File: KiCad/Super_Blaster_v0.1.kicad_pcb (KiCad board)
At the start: 4 copper layers, 27 x 59 mm, 13 parts, among them J1 USB_TypeC_AMP_12401610E4#2A, J2 CONN_02X20, J3 CONN_02X20, J4 CONN_02X20, U1 LM324, U2 iCE40-HX8K-CT256, U3 FUSB340, U4 FT601Q

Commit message: top routed?
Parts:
- removed J3, J4: CONN_02X20, Pin_Headers:Pin_Header_Straight_2x20_Pitch1.27mm
- added C1: .1u, Capacitors_SMD:C_0402, F.Cu at (105.8, 154.0)
- added C2: .1u, Capacitors_SMD:C_0402, F.Cu at (103.7, 156.3)
- added C3: .1u, Capacitors_SMD:C_0402, F.Cu at (122.2, 153.8)
- added C4: .1u, Capacitors_SMD:C_0402, F.Cu at (123.7, 156.9)
- added C5: .1u, Capacitors_SMD:C_0402, F.Cu at (106.4, 157.0)
- added C6: 18p, Capacitors_SMD:C_0402, B.Cu at (116.6, 153.9)
- added C7: 18p, Capacitors_SMD:C_0402, F.Cu at (125.0, 152.4)
- added C9: .1uF, Capacitors_SMD:C_0402, F.Cu at (119.6, 154.0)
- added M1: CLOCK_EN, Crystals:Crystal_SMD_EuroQuartz_MT-4pin_3.2x2.5mm, B.Cu at (114.0, 114.0)
- added R1: 5.1K_10%, Resistors_SMD:R_0402, B.Cu at (112.8, 153.0)
- added R2: ?, Resistors_SMD:R_0402, F.Cu at (125.4, 149.3)
- added R3: ?, Resistors_SMD:R_0402, F.Cu at (123.7, 149.3)
- added R4: ?, Resistors_SMD:R_0402, F.Cu at (121.9, 149.3)
- added R5: ?, Resistors_SMD:R_0402, F.Cu at (120.4, 149.4)
- added R6: 5.1K_10%, Resistors_SMD:R_0402, B.Cu at (114.0, 153.0)
- added R7: 10K, Resistors_SMD:R_0402, F.Cu at (120.7, 151.7)
- added R8: 1.6K 1%, Resistors_SMD:R_0402, F.Cu at (110.1, 147.5)
- added RN1: 1M, Resistors_SMD:R_Array_Concave_4x0402, B.Cu at (104.1, 144.0)
- added Y1: 30MHz, Crystals:Crystal_SMD_MicroCrystal_CC1V-T1A-2pin_8.0x3.7mm, F.Cu at (129.7, 142.8)
- C8: moved to B.Cu
- R10, R9: footprint Resistors_SMD:R_0603 -> Resistors_SMD:R_0402
- moved R10 42.8 mm to (120.5, 157.0), turned to 0 degrees
- moved R9 42.0 mm to (109.6, 153.7), turned to 0 degrees
- moved D1 27.0 mm to (101.7, 153.1), turned to 0 degrees
- moved C8 19.0 mm to (113.1, 155.4), turned to 0 degrees
- moved U3 1.99 mm to (114.7, 144.3), turned to 225 degrees
- moved U2 1.00 mm to (113.5, 115.0), turned to 315 degrees
- moved U4 0.81 mm to (113.5, 134.3), turned to 45 degrees
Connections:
- net /Bottom_Interface/BE_0 renamed Net-(U2-PadN6)
- net /Bottom_Interface/BE_1 renamed Net-(U2-PadT1)
- net /Bottom_Interface/BE_2 renamed Net-(U2-PadP4)
- net /Bottom_Interface/BE_3 renamed Net-(U2-PadR2)
- net /Bottom_Interface/CBSEL_0 renamed /CBSEL_0
- net /Bottom_Interface/CBSEL_1 renamed /CBSEL_1
- net /USB_Connection/1.5A_DET renamed /1.5A_DET
- net /USB_Connection/3A_DET renamed /3A_DET
- net /USB_Connection/BE_0 renamed BE_0
- net /USB_Connection/BE_1 renamed BE_1
- net /USB_Connection/BE_2 renamed BE_2
- net /USB_Connection/BE_3 renamed BE_3
- net /USB_Connection/GPIO0 renamed /GPIO0
- net /USB_Connection/GPIO1 renamed /GPIO1
- net /USB_Connection/SS_RX+ renamed /USB_Connection/SS_RX_P
- net /USB_Connection/SS_RX- renamed /USB_Connection/SS_RX_N
- net /USB_Connection/SS_RX1+ renamed /USB_Connection/SS_RX1_P
- net /USB_Connection/SS_RX1- renamed /USB_Connection/SS_RX1_N
- net /USB_Connection/SS_TX+ renamed /USB_Connection/SS_TX_P
- net /USB_Connection/SS_TX- renamed /USB_Connection/SS_TX_N
- net /USB_Connection/USB_D+ renamed /USB_Connection/USB_D_P
- net /USB_Connection/USB_D- renamed /USB_Connection/USB_D_N
- net /USB_Connection/~SIWU renamed /~SIWU
- J1 pad A10: /USB_Connection/SS_RX2- -> /USB_Connection/SS_RX2_N
- J1 pad A11: /USB_Connection/SS_RX2+ -> /USB_Connection/SS_RX2_P
- J1 pad A2: /USB_Connection/SS_TX1+ -> /USB_Connection/SS_TX1_P
- J1 pad A3: /USB_Connection/SS_TX1- -> /USB_Connection/SS_TX1_N
- J1 pad B2: /USB_Connection/SS_TX2- -> /USB_Connection/SS_TX2_N
- J1 pad B3: /USB_Connection/SS_TX2+ -> /USB_Connection/SS_TX2_P
- R9 pad 2: /Bottom_Interface/~CRESET -> /~CRESET
- U2 pad A12: Net-(U2-PadA12) -> Earth
- U2 pad A4: Net-(U2-PadA12) -> Earth
- U2 pad C15: Net-(U2-PadC15) -> 3v3
- U2 pad E1: Net-(U2-PadE1) -> 3v3
- U2 pad E15: Net-(U2-PadA12) -> Earth
- U2 pad E16: Net-(U2-PadE16) -> D0
- U2 pad E7: Net-(U2-PadE7) -> Earth
- U2 pad F15: Net-(U2-PadF15) -> D2
- U2 pad F16: Net-(U2-PadF16) -> D1
- U2 pad G15: Net-(U2-PadG15) -> D4
- U2 pad G16: Net-(U2-PadG16) -> D3
- U2 pad G6: Net-(U2-PadE1) -> 3v3
- U2 pad G7: Net-(U2-PadA12) -> Earth
- U2 pad G8: Net-(U2-PadA12) -> Earth
- U2 pad G9: Net-(U2-PadA12) -> Earth
- U2 pad H10: Net-(U2-PadC15) -> 3v3
- U2 pad H15: Net-(U2-PadC15) -> 3v3
- U2 pad H7: Net-(U2-PadA12) -> Earth
- U2 pad H8: Net-(U2-PadA12) -> Earth
- U2 pad H9: Net-(U2-PadA12) -> Earth
- U2 pad J15: Net-(U2-PadJ15) -> D6
- U2 pad J16: Net-(U2-PadJ16) -> D5
- U2 pad J6: Net-(U2-PadE1) -> 3v3
- U2 pad J7: Net-(U2-PadA12) -> Earth
- U2 pad J8: Net-(U2-PadA12) -> Earth
- U2 pad J9: Net-(U2-PadA12) -> Earth
- U2 pad K15: Net-(U2-PadK15) -> D8
- U2 pad K16: Net-(U2-PadK16) -> D7
- U2 pad K2: Net-(U2-PadA12) -> Earth
- U2 pad K7: Net-(U2-PadA12) -> Earth
- U2 pad K9: /Bottom_Interface/GBIN4 -> /Bottom_Interface/50MHz
- U2 pad L10: D13 -> Net-(U2-PadL10)
- U2 pad L11: D3 -> Net-(U2-PadL11)
- U2 pad L15: Net-(U2-PadA12) -> Earth
- U2 pad L16: Net-(U2-PadL16) -> D9
- U2 pad L9: D22 -> Net-(U2-PadL9)
- U2 pad M11: D6 -> Net-(U2-PadM11)
- U2 pad M12: D1 -> Net-(U2-PadM12)
- U2 pad M15: Net-(U2-PadM15) -> D11
- U2 pad M16: Net-(U2-PadM16) -> D10
- U2 pad M7: D30 -> Net-(U2-PadM7)
- U2 pad M8: D27 -> Net-(U2-PadM8)
- U2 pad M9: D16 -> Net-(U2-PadM9)
- U2 pad N1: Net-(U2-PadE1) -> 3v3
- U2 pad N10: D11 -> Net-(U2-PadN10)
- U2 pad N11: /Bottom_Interface/~CRESET -> Net-(U2-PadN11)
- U2 pad N12: D4 -> Net-(U2-PadN12)
- U2 pad N15: Net-(U2-PadC15) -> 3v3
- U2 pad N16: Net-(U2-PadN16) -> D12
- U2 pad N5: /Bottom_Interface/~TXE -> Net-(U2-PadN5)
- U2 pad N7: D29 -> Net-(U2-PadN7)
- U2 pad N8: Net-(U2-PadN8) -> Earth
- U2 pad N9: D18 -> Net-(U2-PadN9)
- U2 pad P10: D12 -> Net-(U2-PadP10)
- U2 pad P15: Net-(U2-PadP15) -> D13
- U2 pad P16: Net-(U2-PadP16) -> D14
- U2 pad P5: /Bottom_Interface/~WR -> Net-(U2-PadP5)
- U2 pad P6: D28 -> Net-(U2-PadP6)
- U2 pad P7: D19 -> Net-(U2-PadP7)
- U2 pad P8: D24 -> Net-(U2-PadP8)
- U2 pad P9: D15 -> Net-(U2-PadP9)
- U2 pad R10: D14 -> D22
- U2 pad R15: Net-(U2-PadR15) -> D15
- U2 pad R16: D0 -> D16
- U2 pad R3: /Bottom_Interface/~RD -> Net-(U2-PadR3)
- U2 pad R5: /Bottom_Interface/~OE -> D29
- U2 pad R6: D25 -> D27
- U2 pad R7: Net-(U2-PadA12) -> Earth
- U2 pad T10: D10 -> D23
- U2 pad T11: D9 -> D21
- U2 pad T12: Net-(U2-PadA12) -> Earth
- U2 pad T13: D5 -> D20
- U2 pad T14: D7 -> D19
- U2 pad T15: D8 -> D18
- U2 pad T16: D2 -> D17
- U2 pad T2: /Bottom_Interface/~RXF -> Net-(U2-PadT2)
- U2 pad T3: /Bottom_Interface/~Wakeup -> Net-(U2-PadT3)
- U2 pad T4: Net-(U2-PadA12) -> Earth
- U2 pad T5: D26 -> D30
- U2 pad T6: D23 -> D28
- U2 pad T7: D21 -> D26
- U2 pad T8: D20 -> D25
- U2 pad T9: D17 -> D24
- U4 pad 15: /USB_Connection/~Reset -> /~RESET
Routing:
- net D13: track 0.00 -> 23.4 mm
- net D20: track 0.00 -> 23.0 mm
- net D16: track 0.00 -> 23.0 mm
- net D17: track 0.00 -> 23.0 mm
- net D19: track 0.00 -> 23.0 mm
- net D22: track 0.00 -> 23.0 mm
- net D15: track 0.00 -> 23.0 mm
- net D10: track 0.00 -> 23.0 mm
- net D14: track 0.00 -> 23.0 mm
- net D9: track 0.00 -> 23.0 mm
- net D11: track 0.00 -> 23.0 mm
- net D12: track 0.00 -> 23.0 mm
- net D18: track 0.00 -> 23.0 mm
- net D8: track 0.00 -> 23.0 mm
- net D21: track 0.00 -> 22.9 mm
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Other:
- net class 4mil added: clearance 0.1016, trace_width 0.1016, via_dia 0.45, via_drill 0.3
- net class 5 mil added: clearance 0.127, trace_width 0.127, via_dia 0.45, via_drill 0.3
- net class Data_Bus added: clearance 0.127, trace_width 0.127, via_dia 0.4572, via_drill 0.254
- net class Data_EN added: clearance 0.127, trace_width 0.127, via_dia 0.4572, via_drill 0.254
- net class Default: clearance 0.2 -> 0.1016; trace_width 0.25 -> 0.127; via_dia 0.6 -> 0.4572; via_drill 0.4 -> 0.254
- rule pad_to_mask_clearance: 0.2 -> 0.1
- rule trace_clearance: 0.2 -> 0.1016
- rule trace_min: 0.2 -> 0.1016
- rule via_min_drill: 0.3 -> 0
- rule via_min_size: 0.4 -> 0

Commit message: 10_20_2017 update
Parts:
- added J3: CONN_02X10, Pin_Headers:Pin_Header_Straight_2x10_Pitch1.27mm, F.Cu at (127.2, 101.0)
- added J4: CONN_02X10, Pin_Headers:Pin_Header_Straight_2x10_Pitch1.27mm, F.Cu at (101.5, 114.3)
- J2: value CONN_02X20 -> CONN_02X10; footprint Pin_Headers:Pin_Header_Straight_2x20_Pitch1.27mm -> Pin_Headers:Pin_Header_Straight_2x10_Pitch1.27mm
- M1: footprint Crystals:Crystal_SMD_EuroQuartz_MT-4pin_3.2x2.5mm -> Crystals:Crystal_SMD_2520-4pin_2.5x2.0mm
- U1: footprint SMD_Packages:SOIC-14_N -> Homebrew:Homebrew-HV-QFN-16; moved to B.Cu
- Y1: moved to B.Cu
- moved D1 51.4 mm to (146.1, 127.3), turned to 180 degrees
- moved R1 49.8 mm to (134.0, 108.0)
- moved R7 48.3 mm to (138.3, 106.8)
- moved C7 46.2 mm to (139.6, 108.6)
- moved R10 43.7 mm to (143.3, 119.8), turned to 180 degrees
- moved R9 39.5 mm to (138.2, 126.5), turned to 180 degrees
- moved C9 34.7 mm to (134.6, 122.8), turned to 180 degrees
- moved C4 25.2 mm to (112.6, 134.3), turned to 270 degrees
- moved R3 25.0 mm to (103.4, 134.7), turned to 90 degrees
- moved R2 24.9 mm to (105.3, 134.6), turned to 270 degrees
- moved R6 24.4 mm to (97.2, 135.3)
- moved R5 24.3 mm to (104.7, 130.8)
- moved R4 24.3 mm to (104.7, 132.1), turned to 180 degrees
- moved C2 24.1 mm to (113.4, 134.3), turned to 90 degrees
- moved C1 22.2 mm to (115.4, 134.0), turned to 135 degrees
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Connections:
- net Net-(C1-Pad2) renamed /USB_Connection/T2_N
- net Net-(C2-Pad2) renamed /USB_Connection/T1_N
- net Net-(C3-Pad1) renamed /USB_Connection/T2_P
- net Net-(C4-Pad1) renamed /USB_Connection/T1_P
- net Net-(C6-Pad1) renamed /USB_Connection/Xo
- net Net-(C7-Pad2) renamed /USB_Connection/Xi
- U3 pad 8: /USB_Connection/SS_RX2+ -> /USB_Connection/SS_RX2_P
- U3 pad 9: /USB_Connection/SS_RX2- -> /USB_Connection/SS_RX2_N
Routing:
- net Earth: track 0.00 -> 29.8 mm, vias 0 -> 12
- net /USB_Connection/USB_D_N: track 0.00 -> 20.7 mm
- net /USB_Connection/USB_D_P: track 0.00 -> 19.8 mm, vias 0 -> 2
- net D17: track 23.0 -> 3.38 mm
- net D16: track 23.0 -> 3.54 mm
- net D18: track 23.0 -> 4.34 mm
- net D14: track 23.0 -> 4.92 mm
- net D15: track 23.0 -> 5.13 mm
- net D19: track 23.0 -> 5.31 mm
- net D12: track 23.0 -> 5.95 mm
- net D13: track 23.4 -> 6.41 mm
- net D20: track 23.0 -> 6.28 mm
- net D10: track 23.0 -> 7.09 mm
- net D11: track 23.0 -> 7.45 mm
- net D9: track 23.0 -> 7.87 mm
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- added copper zone on In2.Cu, net 3v3
- added copper zone on In1.Cu, net Earth
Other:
- board size 27 x 59 mm -> 30 x 45 mm
- net class Default: clearance 0.1016 -> 0.127
- rule pad_to_mask_clearance: 0.1 -> 0.0762
- rule trace_clearance: 0.1016 -> 0.127
- board text added: "3.3V power"
- board text added: "VLeft"
- board text added: "VRight"

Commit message: 12_11_17 update
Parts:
- added C10: .1uF, Capacitors_SMD:C_0402, F.Cu at (136.6, 140.4)
- added C11: 1nF, Capacitors_SMD:C_0402, F.Cu at (140.1, 140.4)
- added R11: 1M, Resistors_SMD:R_0402, F.Cu at (133.2, 140.5)
- C6: moved to F.Cu
- Y1: footprint Crystals:Crystal_SMD_MicroCrystal_CC1V-T1A-2pin_8.0x3.7mm -> Crystals:Crystal_SMD_2016-4pin_2.0x1.6mm; moved to F.Cu
- moved C7 32.2 mm to (119.7, 133.9), turned to 135 degrees
- moved Y1 12.8 mm to (120.9, 136.0), turned to 180 degrees
- moved C6 9.10 mm to (120.9, 133.2), turned to 135 degrees
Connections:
- C5 pad 1: Earth -> GND
- C6 pad 1: /USB_Connection/Xo -> GND
- C6 pad 2: Earth -> /USB_Connection/Xo
- C7 pad 1: Earth -> GND
- C8 pad 2: Earth -> GND
- J1 pad A1: Earth -> GND
- J1 pad A12: Earth -> GND
- J1 pad A4: /USB_Connection/USB_V -> USB_V
- J1 pad A9: /USB_Connection/USB_V -> USB_V
- J1 pad B1: Earth -> GND
- J1 pad B12: Earth -> GND
- J1 pad B4: /USB_Connection/USB_V -> USB_V
- J1 pad B9: /USB_Connection/USB_V -> USB_V
- J3 pad 15: Net-(J3-Pad15) -> USB_V
- J3 pad 16: Net-(J3-Pad16) -> USB_V
- J3 pad 17: Net-(J3-Pad17) -> 3v3
- J3 pad 18: Net-(J3-Pad18) -> 3v3
- J3 pad 19: Net-(J3-Pad19) -> GND
- J3 pad 20: Net-(J3-Pad20) -> GND
- R1 pad 2: Earth -> GND
- R6 pad 2: Earth -> GND
- R8 pad 2: Earth -> GND
- U2 pad A12: Earth -> GND
- U2 pad A4: Earth -> GND
- U2 pad E15: Earth -> GND
- U2 pad E7: Earth -> Net-(U2-PadE7)
- U2 pad G7: Earth -> GND
- U2 pad G8: Earth -> GND
- U2 pad G9: Earth -> GND
- U2 pad H7: Earth -> GND
- U2 pad H8: Earth -> GND
- U2 pad H9: Earth -> GND
- U2 pad J7: Earth -> GND
- U2 pad J8: Earth -> GND
- U2 pad J9: Earth -> GND
- U2 pad K2: Earth -> GND
- U2 pad K7: Earth -> GND
- U2 pad L15: Earth -> GND
- U2 pad N8: Earth -> Net-(U2-PadE7)
- U2 pad R7: Earth -> GND
- U2 pad T12: Earth -> GND
- U2 pad T4: Earth -> GND
- U3 pad 12: Earth -> GND
- U3 pad 18: Earth -> GND
- U3 pad 3: Earth -> GND
- U3 pad 7: Earth -> GND
- U3 pad PAD: Earth -> GND
- U4 pad 1: Earth -> GND
- U4 pad 26: Earth -> GND
- U4 pad 29: Earth -> GND
- U4 pad 36: Earth -> GND
- U4 pad 77: Earth -> GND
- Y1 pad 1: /USB_Connection/Xi -> /USB_Connection/Xo
- Y1 pad 2: /USB_Connection/Xo -> GND
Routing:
- net Earth: track 29.8 -> 0.00 mm, vias 12 -> 0
- net GND: track 0.00 -> 28.7 mm, vias 0 -> 10
- net /USB_Connection/Xi: track 0.00 -> 6.24 mm
- net /USB_Connection/Xo: track 0.00 -> 5.50 mm
- net /USB_Connection/USB_D_N: track 20.7 -> 22.6 mm
- net /USB_Connection/USB_D_P: track 19.8 -> 21.5 mm
- net Net-(U2-PadE7): track 0.00 -> 1.07 mm, vias 0 -> 2
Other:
- net class Default: clearance 0.127 -> 0.1524
- rule trace_clearance: 0.127 -> 0.1524

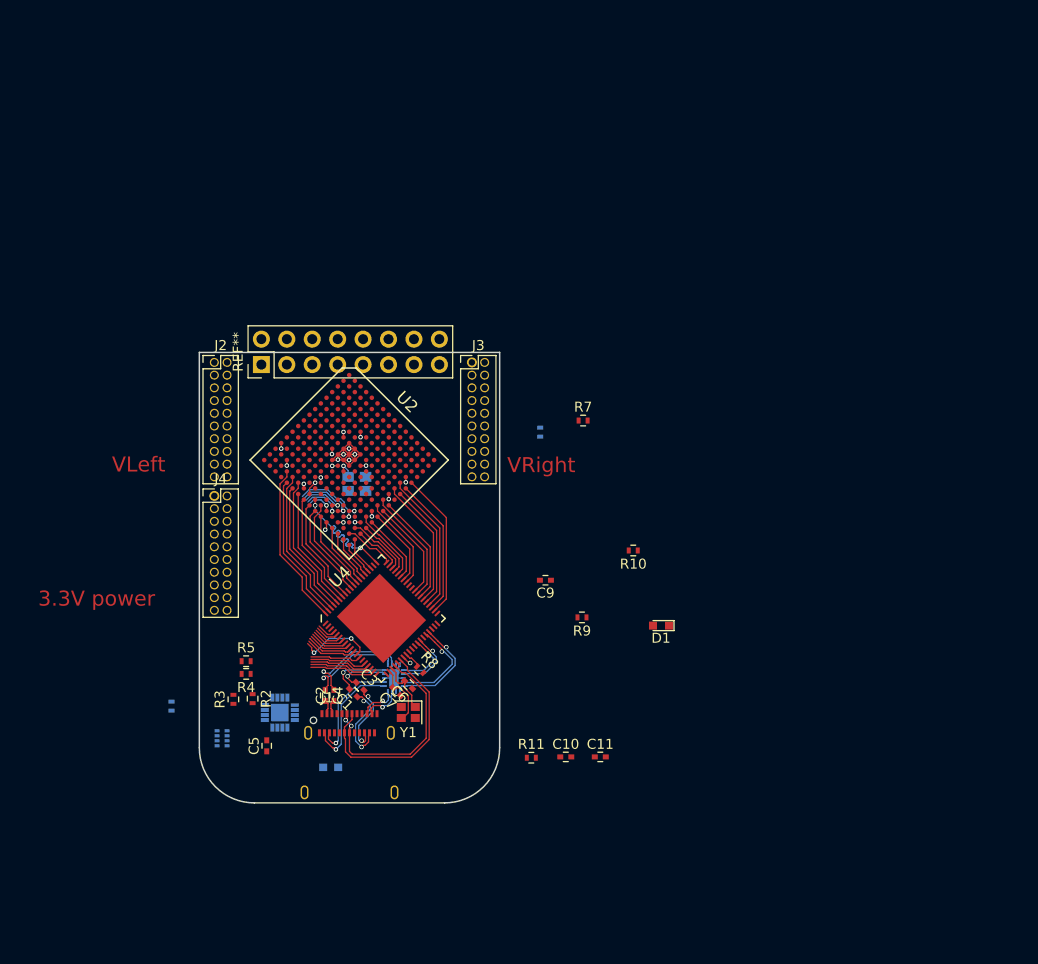
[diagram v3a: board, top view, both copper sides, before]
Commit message: switch to beaglepocket outline
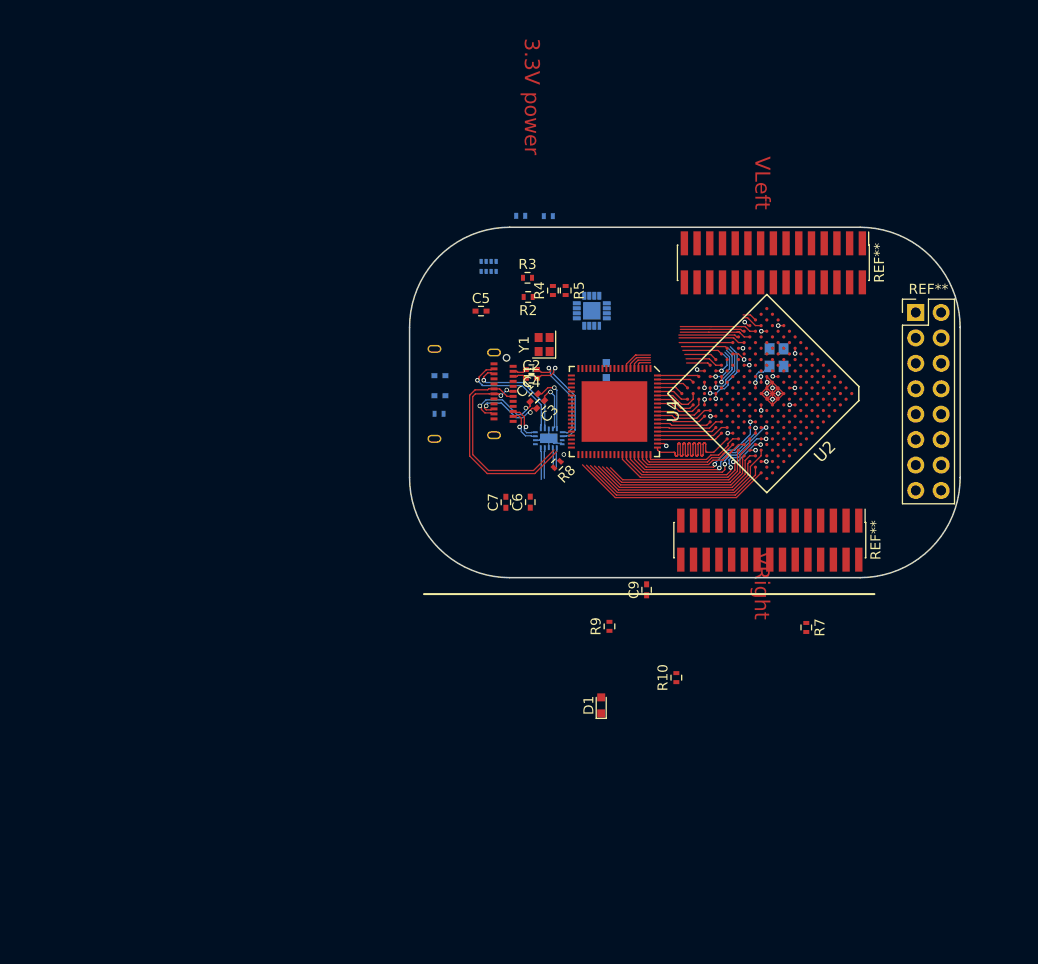
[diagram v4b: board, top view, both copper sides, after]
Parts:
- removed J2, J3, J4: CONN_02X10, Pin_Headers:Pin_Header_Straight_2x10_Pitch1.27mm
- added REF**: Pin_Header_Straight_2x15_Pitch1.27mm_SMD, Pin_Headers:Pin_Header_Straight_2x15_Pitch1.27mm_SMD, F.Cu at (157.3, 91.1)
- added REF**: Pin_Header_Straight_2x15_Pitch1.27mm_SMD, Pin_Headers:Pin_Header_Straight_2x15_Pitch1.27mm_SMD, F.Cu at (157.0, 118.8)
- C10, C11, R11: moved to B.Cu
- moved REF** 65.6 mm to (171.6, 96.0), turned to 0 degrees
- moved R6 60.1 mm to (132.1, 86.4), turned to 180 degrees
- moved RN1 54.1 mm to (128.9, 91.4), turned to 270 degrees
- moved R3 51.3 mm to (132.8, 92.5), turned to 0 degrees
- moved U1 50.8 mm to (139.2, 95.8), turned to 180 degrees
- moved R4 49.1 mm to (135.3, 93.8), turned to 90 degrees
- moved R5 48.9 mm to (136.6, 93.8), turned to 270 degrees
- moved R2 48.7 mm to (132.8, 94.5), turned to 180 degrees
- moved C5 48.4 mm to (128.1, 95.9), turned to 0 degrees
- moved C8 48.3 mm to (140.7, 101.8), turned to 90 degrees
- moved M1 43.8 mm to (157.7, 100.5), turned to 270 degrees
- moved U2 42.2 mm to (156.7, 104.1), turned to 225 degrees
- moved C11 41.3 mm to (124.0, 102.3), turned to 180 degrees
- moved Y1 39.2 mm to (134.4, 99.2), turned to 90 degrees
- moved C4 38.5 mm to (133.2, 101.7), turned to 180 degrees
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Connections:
- C9 pad 2: Earth -> GND
- M1 pad 2: Earth -> GND
- R3 pad 2: Earth -> GND
- R5 pad 2: Earth -> GND
- RN1 pad 3: Earth -> GND
- U1 pad 11: Earth -> GND
- U2 pad B16: Net-(U2-PadB16) -> D0
- U2 pad C16: Net-(U2-PadC16) -> D1
- U2 pad D14: Net-(U2-PadD14) -> D2
- U2 pad D15: Net-(U2-PadD15) -> D4
- U2 pad D16: Net-(U2-PadD16) -> D3
- U2 pad E13: Net-(U2-PadE13) -> D9
- U2 pad E14: Net-(U2-PadE14) -> D8
- U2 pad E16: D0 -> D5
- U2 pad F12: Net-(U2-PadF12) -> D10
- U2 pad F13: Net-(U2-PadF13) -> D11
- U2 pad F14: Net-(U2-PadF14) -> D6
- U2 pad F15: D2 -> D13
- U2 pad F16: D1 -> D7
- U2 pad G12: Net-(U2-PadG12) -> D12
- U2 pad G15: D4 -> D15
- U2 pad G16: D3 -> D14
- U2 pad H16: Net-(U2-PadH16) -> /Bottom_Interface/CLK
- U2 pad J15: D6 -> D17
- U2 pad J16: D5 -> D16
- U2 pad K15: D8 -> D19
- U2 pad K16: D7 -> D18
- U2 pad L16: D9 -> D20
- U2 pad M15: D11 -> D22
- U2 pad M16: D10 -> D21
- U2 pad N11: Net-(U2-PadN11) -> /~CRESET
- U2 pad N16: D12 -> D23
- U2 pad P15: D13 -> D24
- U2 pad P16: D14 -> D25
- U2 pad R10: D22 -> Net-(U2-PadR10)
- U2 pad R15: D15 -> D26
- U2 pad R16: D16 -> D27
- U2 pad R4: D31 -> Net-(U2-PadR4)
- U2 pad R5: D29 -> Net-(U2-PadR5)
- U2 pad R6: D27 -> Net-(U2-PadR6)
- U2 pad R9: /Bottom_Interface/CLK -> Net-(U2-PadR9)
- U2 pad T10: D23 -> Net-(U2-PadT10)
- U2 pad T11: D21 -> Net-(U2-PadT11)
- U2 pad T13: D20 -> D31
- U2 pad T14: D19 -> D30
- U2 pad T15: D18 -> D29
- U2 pad T16: D17 -> D28
- U2 pad T5: D30 -> Net-(U2-PadT5)
- U2 pad T6: D28 -> Net-(U2-PadT6)
- U2 pad T7: D26 -> Net-(U2-PadT7)
- U2 pad T8: D25 -> Net-(U2-PadT8)
- U2 pad T9: D24 -> Net-(U2-PadT9)
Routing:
- net D31: track 16.4 -> 4.18 mm
- net D29: track 15.1 -> 3.18 mm
- net D30: track 14.8 -> 3.68 mm
- net D28: track 13.6 -> 2.68 mm
- net D27: track 14.0 -> 3.32 mm
- net D10: track 7.09 -> 17.4 mm, vias 0 -> 2
- net D9: track 7.87 -> 17.9 mm, vias 0 -> 2
- net D12: track 5.95 -> 15.2 mm, vias 0 -> 2
- net /Bottom_Interface/CLK: track 13.2 -> 22.0 mm, vias 2 -> 0
- net D11: track 7.45 -> 15.9 mm, vias 0 -> 2
- net D8: track 9.45 -> 17.6 mm, vias 0 -> 2
- net Net-(U2-PadR4): track 0.00 -> 7.70 mm
- net /Bottom_Interface/~RD: track 7.57 -> 0.00 mm, vias 2 -> 0
- net Net-(U2-PadR5): track 0.00 -> 7.55 mm
- net D26: track 12.2 -> 4.71 mm
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- added copper zone on In1.Cu, net GND
- removed copper zone on In1.Cu, net Earth
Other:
- board size 30 x 45 mm -> 55 x 35 mm

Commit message: updates & Bottom sch recovery
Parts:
- C10, C11, C8, M1, R1, R11, R6, RN1, U1, U3: moved to F.Cu
- moved R6 32.6 mm to (128.9, 118.8)
- moved R1 32.0 mm to (128.9, 117.8)
- moved RN1 27.7 mm to (131.4, 119.0), turned to 0 degrees
- moved R4 26.7 mm to (126.8, 119.1), turned to 180 degrees
- moved R5 25.9 mm to (126.8, 117.8), turned to 0 degrees
- moved U1 24.2 mm to (135.1, 119.7), turned to 270 degrees
- moved R3 24.0 mm to (132.4, 116.5), turned to 90 degrees
- moved R2 22.0 mm to (134.3, 116.5), turned to 270 degrees
- moved C7 15.7 mm to (138.7, 101.5), turned to 270 degrees
- moved C5 14.6 mm to (142.2, 99.5), turned to 270 degrees
- moved M1 12.9 mm to (170.3, 97.8), turned to 180 degrees
- moved C6 12.2 mm to (136.8, 103.4), turned to 0 degrees
- moved C8 9.59 mm to (150.2, 102.0), turned to 0 degrees
- moved R11 9.07 mm to (122.7, 97.2), turned to 180 degrees
- moved C1 8.72 mm to (126.9, 110.4), turned to 270 degrees
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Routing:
- net /USB_Connection/USB_D_N: track 21.3 -> 0.00 mm
- net /USB_Connection/USB_D_P: track 20.2 -> 0.00 mm, vias 2 -> 0
- net /Bottom_Interface/CLK: track 22.0 -> 7.68 mm
- net /USB_Connection/SS_RX1_P: track 12.0 -> 0.00 mm, vias 1 -> 0
- net /USB_Connection/T1_N: track 11.1 -> 0.00 mm, vias 1 -> 0
- net /USB_Connection/SS_RX1_N: track 11.1 -> 0.00 mm, vias 1 -> 0
- net /USB_Connection/T1_P: track 10.1 -> 0.00 mm, vias 1 -> 0
- net /USB_Connection/SS_TX2_N: track 8.67 -> 0.00 mm, vias 2 -> 0
- net /USB_Connection/SS_TX2_P: track 7.76 -> 0.00 mm, vias 2 -> 0
- net Net-(U2-PadH11): track 0.00 -> 6.26 mm, vias 0 -> 1
- net /USB_Connection/T2_N: track 6.12 -> 0.00 mm, vias 1 -> 0
- net /USB_Connection/T2_P: track 5.13 -> 0.00 mm, vias 1 -> 0
- net GND: track 29.0 -> 24.5 mm, vias 11 -> 12
- net /USB_Connection/SS_RX2_P: track 4.04 -> 0.00 mm, vias 1 -> 0
- net /USB_Connection/SS_RX2_N: track 4.04 -> 0.00 mm, vias 1 -> 0
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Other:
- net class 10 mil added: clearance 0.1524, trace_width 0.254, via_dia 0.4572, via_drill 0.254
- net class 4mil removed
- net class USB_Super_diff added: clearance 0.127, trace_width 0.233375, via_dia 0.4572, via_drill 0.254
